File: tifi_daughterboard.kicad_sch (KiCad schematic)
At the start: 30 parts, among them J1 SSW-110-23-F-D, J2 SSW-110-23-F-D, J3 SM04B-SRSS-TB(LF)(SN), J4 SSW-103-02-T-S-RA, J5 PH2-04-UA, Q1 BSS138LT1G, U1 SGP40-D-R4, U2 SHT40-AD1B-R3

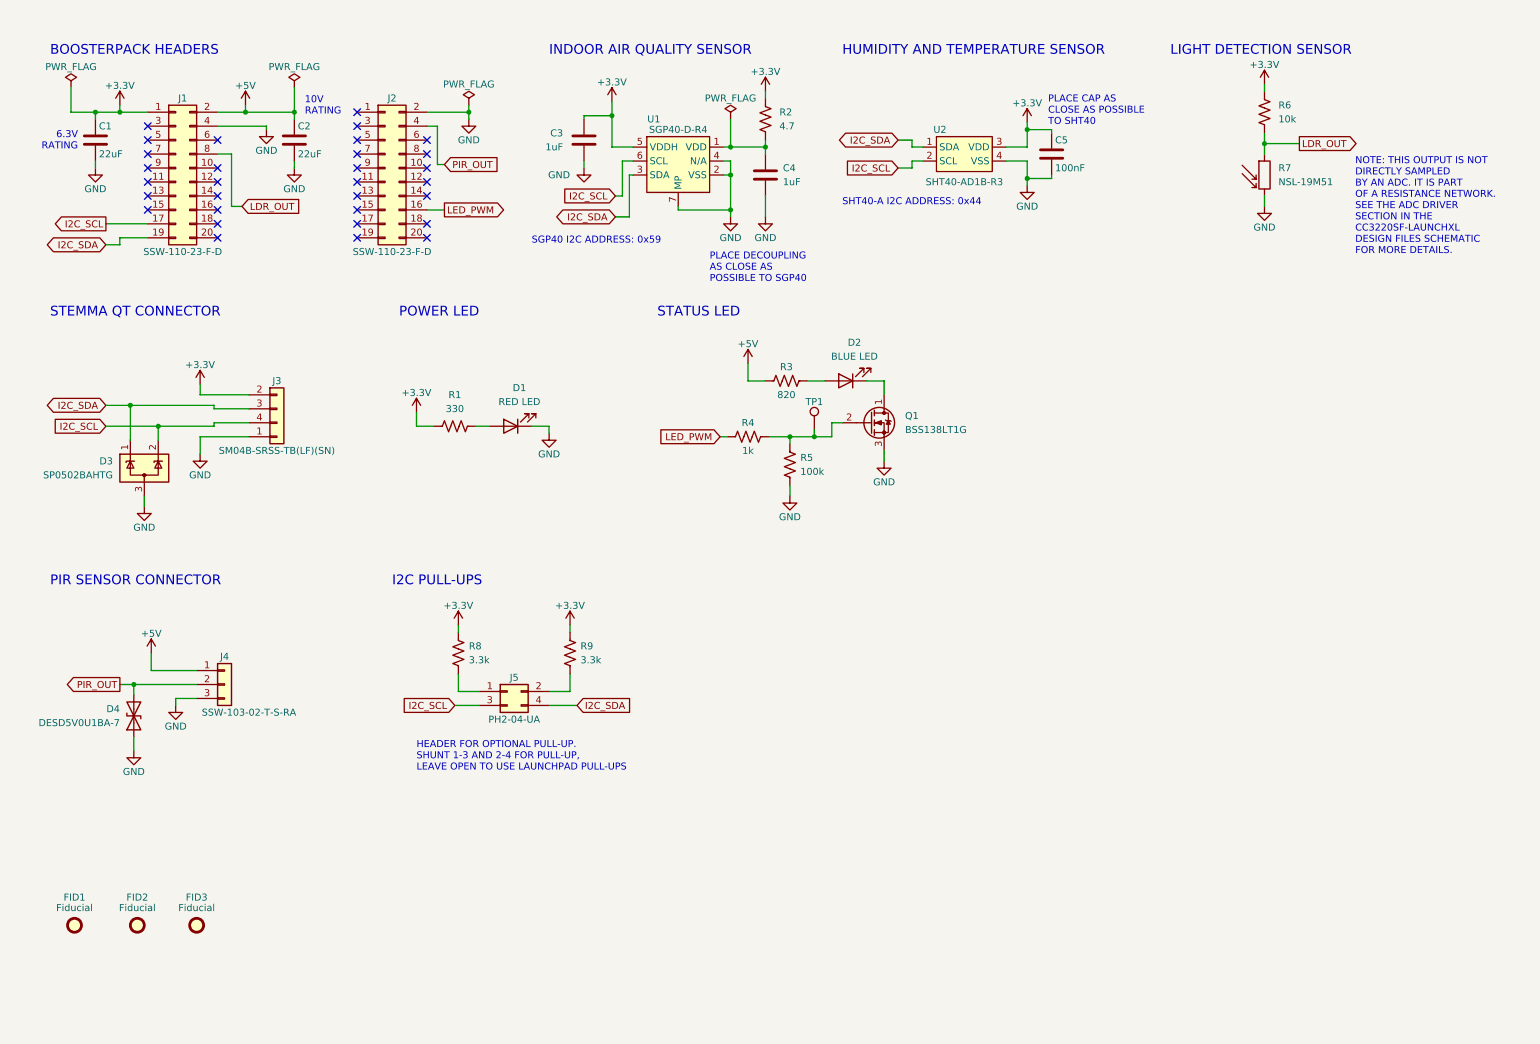
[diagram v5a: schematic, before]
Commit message: Schematic cleanup, minor board fixes.
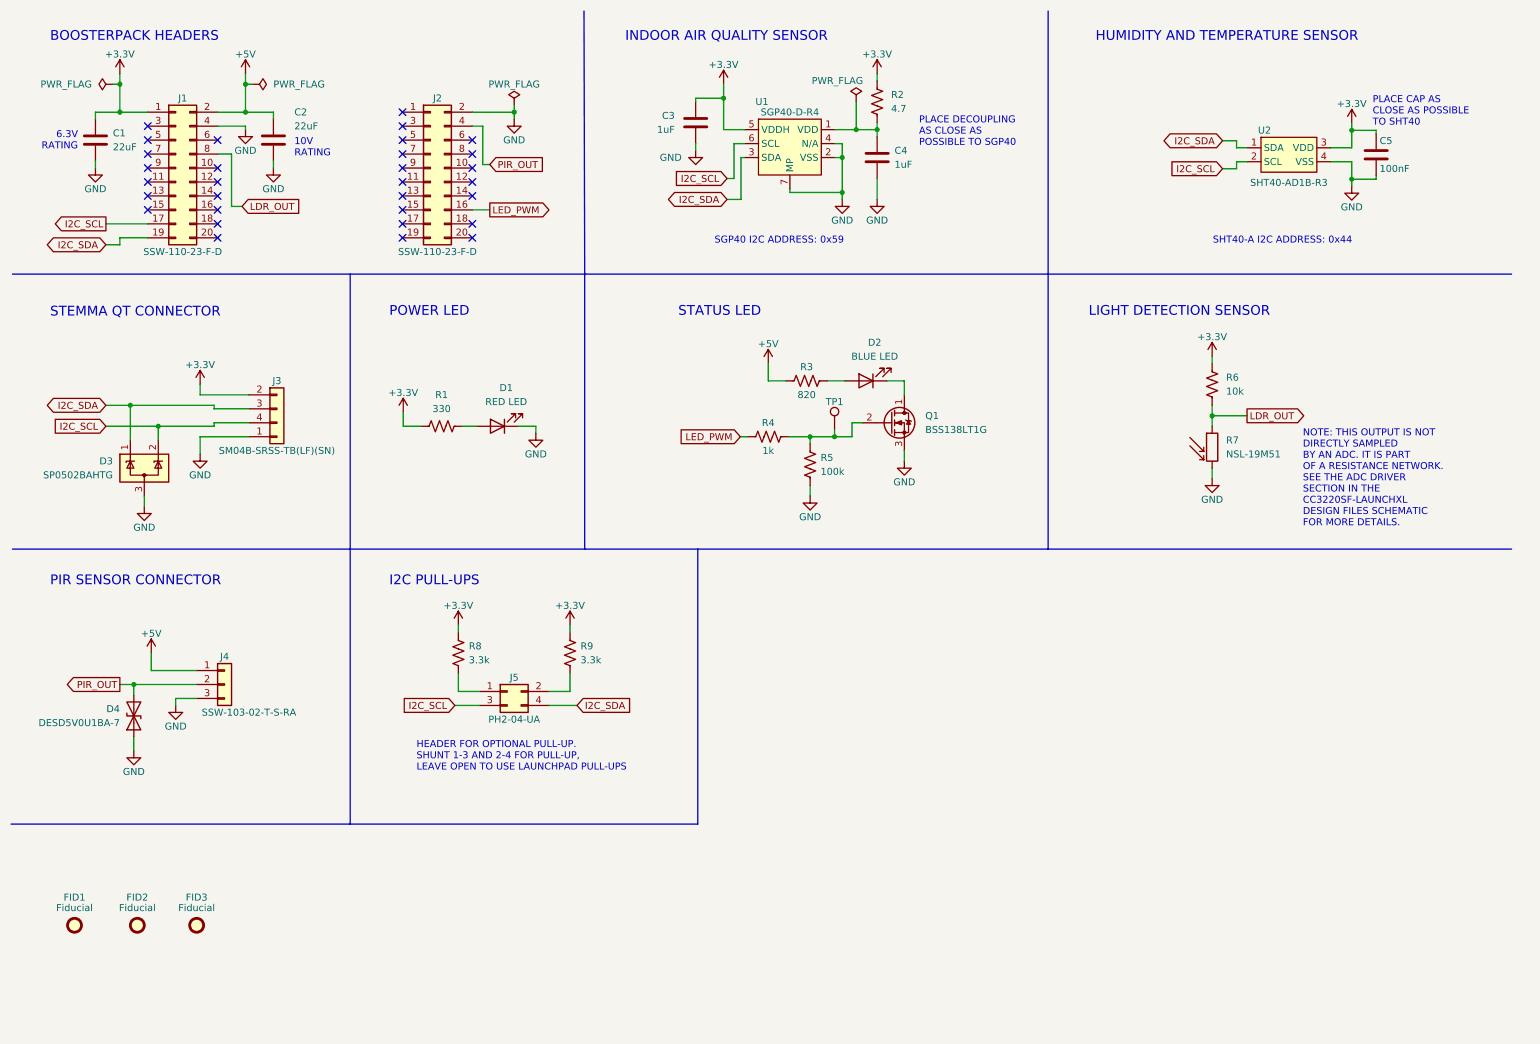
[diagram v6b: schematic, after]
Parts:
- Q1: footprint Package_TO_SOT_SMD:SOT-23W -> Package_TO_SOT_SMD:SOT-23
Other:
- moved on the sheet: C2, C3, C4, C5, D1, D2, J2, Q1, R1, R2, R3, R4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

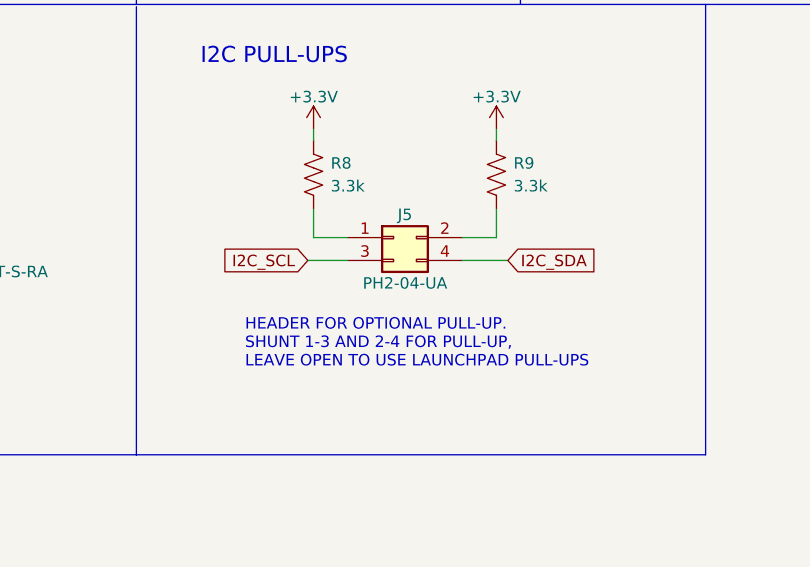
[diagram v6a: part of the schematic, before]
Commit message: Add purchase links for each component.
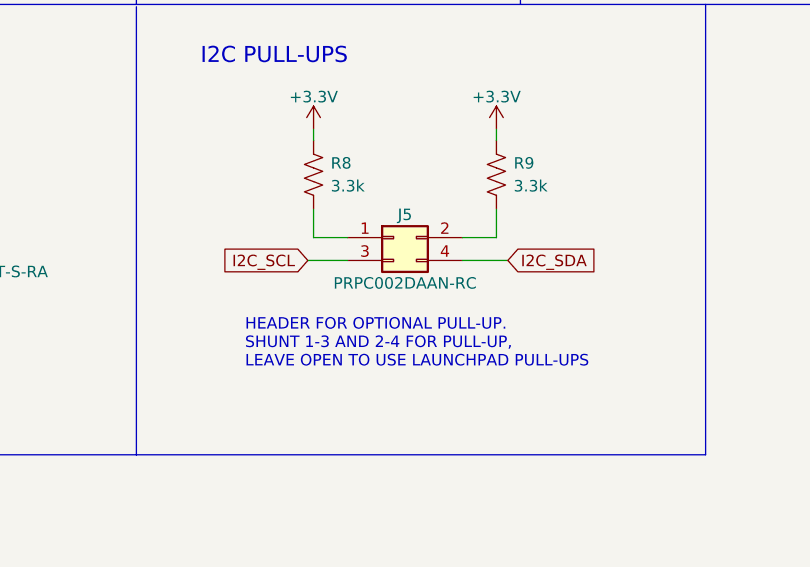
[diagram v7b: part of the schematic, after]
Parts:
- C3, C4, C5: Supplier Link (none) -> https://www.digikey.com/en/products/detail/samsung-electro-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
- D1, D2: Supplier Link (none) -> https://www.digikey.com/en/products/detail/w%C3%BCrth-elekt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
- D3: Supplier Link (none) -> https://www.digikey.com/en/products/detail/littelfuse-inc/S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
- D4: Supplier Link (none) -> https://www.digikey.com/en/products/detail/diodes-incorpora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
- J1, J2, J4: Supplier Link (none) -> https://www.digikey.com/en/products/detail/samtec-inc/SSW-1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
- J3: Supplier Link (none) -> https://www.newark.com/jst-japan-solderless-terminals/sm04b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
- J5: value PH2-04-UA -> PRPC002DAAN-RC; Supplier Link (none) -> https://www.digikey.com/en/products/detail/sullins-connecto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
- R1, R2, R3, R4, R5, R6, R8, R9: Supplier Link (none) -> https://www.digikey.com/en/products/detail/stackpole-electr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
- R7: Supplier Link (none) -> https://www.digikey.com/en/products/detail/advanced-photoni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
- U1: Supplier Link (none) -> https://www.digikey.com/en/products/detail/sensirion-ag/SGP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
- U2: Supplier Link (none) -> https://www.digikey.com/en/products/detail/sensirion-ag/SHT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
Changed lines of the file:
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@@
+      (effects (font (size 1.27 1.27)) hide)
+    )
+    (property "Supplier Link" "https://www.digikey.com/en/products/detail/samtec-inc/SSW-110-23-F-D/6692909" (id 4) (at 88.265 40.64 0)
       (effects (font (size 1.27 1.27)) hide)
     )
@@
       (effects (font (size 1.27 1.27)) hide)
     )
+    (property "Supplier Link" "https://www.digikey.com/en/products/detail/samtec-inc/SSW-103-02-T-S-RA/5639669" (id 4) (at 50.8 134.62 0)
+      (effects (font (size 1.27 1.27)) hide)
+    )
     (pin "1")
     (pin "2")
@@
       (effects (font (size 1.27 1.27)) hide)
     )
+    (property "Supplier Link" "https://www.digikey.com/en/products/detail/sensirion-ag/SGP40-D-R4/12820418?s=N4IgTCBcDaIMoHEAKAWADAWgCIYEopAF0BfIA" (id 4) (at 153.67 36.83 0)
+      (effects (font (size 1.27 1.27)) hide)
+    )
     (pin "1")
     (pin "2")
@@
     (in_bom yes) (on_board yes)
     (property "Reference" "J5" (id 0) (at 103.505 133.35 0))
-    (property "Value" "PH2-04-UA" (id 1) (at 103.505 140.97 0))
+    (property "Value" "PRPC002DAAN-RC" (id 1) (at 103.505 140.97 0))
     (property "Footprint" "Connector_PinHeader_2.54mm:PinHeader_2x02_P2.54mm_Vertical" (id 2) (at 102.235 135.89 0)
       (effects (font (size 1.27 1.27)) hide)
     )
     (property "Datasheet" "https://app.adam-tech.com/products/download/data_sheet/202065/ph2-xx-ua-data-sheet.pdf" (id 3) (at 102.235 135.89 0)
+      (effects (font (size 1.27 1.27)) hide)
+    )
+    (property "Supplier Link" "https://www.digikey.com/en/products/detail/sullins-connector-solutions/PRPC002DAAN-RC/2775292" (id 4) (at 102.235 135.89 0)
       (effects (font (size 1.27 1.27)) hide)
     )
@@
       (effects (font (size 1.27 1.27)) hide)
     )
+    (property "Supplier Link" "https://www.digikey.com/en/products/detail/sensirion-ag/SHT40-AD1B-R3/14322709?s=N4IgTCBcDaIMoAkAqAWADAWgIIBECMAQhgEoDMIAugL5A" (id 4) (at 244.475 38.227 0)
+      (effects (font (size 1.27 1.27)) hide)
+    )
     (pin "1")
     (pin "2")
@@
       (effects (font (size 1.27 1.27)) hide)
     )
+    (property "Supplier Link" "https://www.digikey.com/en/products/detail/samsung-electro-mechanics/CL21B104KACNNNC/3886757" (id 4) (at 260.35 38.227 0)
+      (effects (font (size 1.27 1.27)) hide)
+    )
     (pin "1")
     (pin "2")
@@
       (effects (font (size 1.27 1.27)) hide)
     )
+    (property "Supplier Link" "https://www.digikey.com/en/products/detail/littelfuse-inc/SP0502BAHTG/1154307?s=N4IgTCBcDaIMoAUAMBWJYBCBBAEgFQHEQBdAXyA" (id 4) (at 36.195 95.25 0)
+      (effects (font (size 1.27 1.27)) hide)
+    )
     (pin "3")
     (pin "1")
@@
       (effects (font (size 1.27 1.27)) hide)
     )
+    (property "Supplier Link" "https://www.digikey.com/en/products/detail/stackpole-electronics-inc/RMCF0805FT3K30/1760325" (id 4) (at 113.665 128.905 0)
+      (effects (font (size 1.27 1.27)) hide)
+    )
     (pin "1")
     (pin "2")
@@
     )
     (property "Datasheet" "~" (id 3) (at 169.545 38.735 0)
+      (effects (font (size 1.27 1.27)) hide)
+    )
+    (property "Supplier Link" "https://www.digikey.com/en/products/detail/samsung-electro-mechanics/CL21B105KAFNNNE/3886724" (id 4) (at 169.545 38.735 0)
       (effects (font (size 1.27 1.27)) hide)
     )
@@
       (effects (font (size 1.27 1.27)) hide)
     )
+    (property "Supplier Link" "https://www.digikey.com/en/products/detail/stackpole-electronics-inc/RMCF0805FT3K30/1760325" (id 4) (at 93.345 128.905 0)
+      (effects (font (size 1.27 1.27)) hide)
+    )
     (pin "1")
     (pin "2")
@@
     )
     (property "Datasheet" "~" (id 3) (at 157.353 94.615 0)
+      (effects (font (size 1.27 1.27)) hide)
+    )
+    (property "Supplier Link" "https://www.digikey.com/en/products/detail/stackpole-electronics-inc/RMCF0805FT100K/1760712" (id 4) (at 157.353 94.615 0)
       (effects (font (size 1.27 1.27)) hide)
     )
@@
       (effects (font (size 1.27 1.27)) hide)
     )
+    (property "Supplier Link" "https://www.digikey.com/en/products/detail/stackpole-electronics-inc/RMCF0805FT820R/1760419" (id 4) (at 156.718 79.375 0)
+      (effects (font (size 1.27 1.27)) hide)
+    )
     (pin "1")
     (pin "2")
@@
     )
     (property "Datasheet" "~" (id 3) (at 169.545 28.575 0)
+      (effects (font (size 1.27 1.27)) hide)
+    )
+    (property "Supplier Link" "https://www.digikey.com/en/products/detail/stackpole-electronics-inc/RMCF0805FT4R70/1760199" (id 4) (at 169.545 28.575 0)
       (effects (font (size 1.27 1.27)) hide)
     )
@@
     )
     (property "Datasheet" "https://www.we-online.com/katalog/datasheet/150080BS75000.pdf" (id 3) (at 167.513 79.375 0)
+      (effects (font (size 1.27 1.27)) hide)
+    )
+    (property "Supplier Link" "https://www.digikey.com/en/products/detail/w%C3%BCrth-elektronik/150080BS75000/4489912?s=N4IgTCBcDaIIwFYAMSAcSBCBlA7MlIAugL5A" (id 4) (at 167.513 79.375 0)
       (effects (font (size 1.27 1.27)) hide)
     )
@@
       (effects (font (size 1.27 1.27)) hide)
     )
+    (property "Supplier Link" "https://www.newark.com/jst-japan-solderless-terminals/sm04b-srss-tb-lf-sn/connector-header-1mm-4-position/dp/87R0314" (id 4) (at 60.325 84.455 0)
+      (effects (font (size 1.27 1.27)) hide)
+    )
     (pin "1")
     (pin "2")
@@
     )
     (property "Datasheet" "~" (id 3) (at 230.505 80.01 0)
+      (effects (font (size 1.27 1.27)) hide)
+    )
+    (property "Supplier Link" "https://www.digikey.com/en/products/detail/stackpole-electronics-inc/RMCF0805FT10K0/1760676" (id 4) (at 230.505 80.01 0)
       (effects (font (size 1.27 1.27)) hide)
     )
@@
       (effects (font (size 1.27 1.27)) hide)
     )
+    (property "Supplier Link" "https://www.digikey.com/en/products/detail/stackpole-electronics-inc/RMCF0805JT1K00/1757881" (id 4) (at 149.733 89.535 0)
+      (effects (font (size 1.27 1.27)) hide)
+    )
     (pin "1")
     (pin "2")
@@
       (effects (font (size 1.27 1.27)) hide)
     )
+    (property "Supplier Link" "https://www.digikey.com/en/products/detail/w%C3%BCrth-elektronik/150080RS75000/4489918?s=N4IgTCBcDaIIwFYAMSAcSBKBlA7MlIAugL5A" (id 4) (at 100.457 87.63 0)
+      (effects (font (size 1.27 1.27)) hide)
+    )
     (pin "1")
     (pin "2")
@@
       (effects (font (size 1.27 1.27)) hide)
     )
+    (property "Supplier Link" "https://www.digikey.com/en/products/detail/diodes-incorporated/DESD5V0U1BA-7/5371876?s=N4IgTCBcDaICIFEDKcCsA1ADAVQIwCEBBAWgHYQBdAXyA" (id 4) (at 34.29 140.335 0)
+      (effects (font (size 1.27 1.27)) hide)
+    )
     (pin "1")
     (pin "2")
@@
     )
     (property "Datasheet" "~" (id 3) (at 136.525 32.385 0)
+      (effects (font (size 1.27 1.27)) hide)
+    )
+    (property "Supplier Link" "https://www.digikey.com/en/products/detail/samsung-electro-mechanics/CL21B105KAFNNNE/3886724" (id 4) (at 136.525 32.385 0)
       (effects (font (size 1.27 1.27)) hide)
     )
@@
     )
     (property "Datasheet" "~" (id 3) (at 41.91 40.64 0)
+      (effects (font (size 1.27 1.27)) hide)
+    )
+    (property "Supplier Link" "https://www.digikey.com/en/products/detail/samtec-inc/SSW-110-23-F-D/6692909" (id 4) (at 41.91 40.64 0)
       (effects (font (size 1.27 1.27)) hide)
     )
@@
       (effects (font (size 1.27 1.27)) hide)
     )
+    (property "Supplier Link" "https://www.digikey.com/en/products/detail/stackpole-electronics-inc/RMCF0805FT330R/1760484" (id 4) (at 90.297 87.63 0)
+      (effects (font (size 1.27 1.27)) hide)
+    )
     (pin "1")
     (pin "2")
@@
     )
     (property "Datasheet" "https://media.digikey.com/pdf/Data%20Sheets/Photonic%20Detetectors%20Inc%20PDFs/NSL-19M51_rev01-04-16.pdf" (id 3) (at 230.505 92.71 0)
+      (effects (font (size 1.27 1.27)) hide)
+    )
+    (property "Supplier Link" "https://www.digikey.com/en/products/detail/advanced-photonix/NSL-19M51/5039794?s=N4IgTCBcDaIHIGUAyBaAjATgLIFY0gF0BfIA" (id 4) (at 230.505 91.44 0)
       (effects (font (size 1.27 1.27)) hide)
     )
@@
     )
     (path "/24d99b1f-8263-434d-8701-ec69034d2fda"
-      (reference "J5") (unit 1) (value "PH2-04-UA") (footprint "Connector_PinHeader_2.54mm:PinHeader_2x02_P2.54mm_Vertical")
+      (reference "J5") (unit 1) (value "PRPC002DAAN-RC") (footprint "Connector_PinHeader_2.54mm:PinHeader_2x02_P2.54mm_Vertical")
     )
     (path "/a693ce77-e4fb-4d3a-afc5-f19cee5f74f8"

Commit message: Licensing
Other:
- note added: "FIDUCIALS"
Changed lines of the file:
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@@
   (title_block
     (title "TI-FI DAUGHTERBOARD")
+    (date "2022-10-05")
     (rev "0")
     (company "UNIVERSITY OF SOUTH CAROLINA")
-    (comment 1 "<LICENSE URL HERE>")
-    (comment 2 "LICENSE: <LICENSE TITLE HERE>")
+    (comment 1 "https://opensource.org/licenses/MIT")
+    (comment 2 "LICENSE: MIT LICENSE")
   )
   (junction (at 255.905 33.782) (diameter 0) (color 0 0 0 0)
@@
     (stroke (width 0) (type default) (color 0 0 0 0))
   )
+  (polyline (pts (xy 73.66 160.02) (xy 73.66 198.12))
+    (stroke (width 0) (type default) (color 0 0 0 0))
+  )
   (polyline (pts (xy 73.66 110.236) (xy 73.66 160.02))
     (stroke (width 0) (type default) (color 0 0 0 0))
@@
     (effects (font (size 1.27 1.27)) (justify left bottom))
   )
+  (text "FIDUCIALS" (at 19.05 166.116 0)
+    (effects (font (size 1.778 1.778)) (justify left bottom))
+  )
   (text "I2C PULL-UPS" (at 80.772 116.84 0)
